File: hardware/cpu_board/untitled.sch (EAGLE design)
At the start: 75 parts, among them IC1 MAX232ECWE, IC2 MAX232ECWE, IC3 AM29F040J, IC4 74HCT138D, IC5 LM2596S, IC6 74HCT273DW, IC7 74LVC1G08DBV, IC8 74LVC1G04DBV, J2 POWER_JACKSLT, U1 AS6C4008-55SIN

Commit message: RAM/ROM address decoder (work in progress)
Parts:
- added IC9: 74HCT138D, 74xx-eu:74HCT138D
- added LED1: (no value), led:LEDCHIP-LED0603
- added R17, R18: (no value), rcl:R-EU_R0603
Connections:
- new net N$46: IC6A.Q4, R17.2
- new net N$47: LED1.A, R17.1
- new net N$48: IC9A.G1, R18.1
- net !MEMEN: now also IC9A.G2A
- net !RAM_CS: now also IC9A.Y2, IC9A.Y4, IC9A.Y5
- net !ROM_CS: now also IC9A.Y0
- net 5V: now also IC9P.VCC, R18.2
- net GND: now also IC9A.A, IC9A.G2B, IC9P.GND, LED1.C
- net ROMSHADOW: now also IC9A.B
- net _A15: now also IC9A.C
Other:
- moved on the sheet: R16
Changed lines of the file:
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@@
 <part name="R16" library="rcl" deviceset="R-EU_" device="R0603"/>
 <part name="IC7" library="74xx-little-de" deviceset="74*1G08" device="DBV" technology="LVC"/>
+<part name="R17" library="rcl" deviceset="R-EU_" device="R0603"/>
+<part name="LED1" library="led" deviceset="LED" device="CHIP-LED0603"/>
+<part name="GND22" library="supply1" deviceset="GND" device=""/>
+<part name="IC9" library="74xx-eu" deviceset="74*138" device="D" technology="HCT"/>
+<part name="GND23" library="supply1" deviceset="GND" device=""/>
+<part name="R18" library="rcl" deviceset="R-EU_" device="R0603"/>
 </parts>
 <sheets>
@@
 <instance part="IC8" gate="A" x="182.88" y="274.32"/>
 <instance part="IC8" gate="P" x="25.4" y="190.5"/>
-<instance part="R16" gate="G$1" x="-220.98" y="-50.8"/>
+<instance part="R16" gate="G$1" x="-210.82" y="-38.1"/>
 <instance part="IC7" gate="A" x="203.2" y="271.78"/>
 <instance part="IC7" gate="P" x="35.56" y="190.5"/>
+<instance part="R17" gate="G$1" x="284.48" y="287.02" rot="R180"/>
+<instance part="LED1" gate="G$1" x="294.64" y="287.02" rot="R90"/>
+<instance part="GND22" gate="1" x="302.26" y="281.94"/>
+<instance part="IC9" gate="A" x="-182.88" y="-40.64"/>
+<instance part="GND23" gate="1" x="-203.2" y="-55.88"/>
+<instance part="R18" gate="G$1" x="-200.66" y="-25.4" rot="R90"/>
+<instance part="IC9" gate="P" x="45.72" y="190.5"/>
 </instances>
 <busses>
@@
 <wire x1="35.56" y1="180.34" x2="35.56" y2="182.88" width="0.1524" layer="91"/>
 <junction x="25.4" y="180.34"/>
+<pinref part="IC9" gate="P" pin="GND"/>
+<wire x1="35.56" y1="180.34" x2="45.72" y2="180.34" width="0.1524" layer="91"/>
+<wire x1="45.72" y1="180.34" x2="45.72" y2="182.88" width="0.1524" layer="91"/>
+<junction x="35.56" y="180.34"/>
 </segment>
 <segment>
@@
 <junction x="248.92" y="276.86"/>
 </segment>
+<segment>
+<pinref part="LED1" gate="G$1" pin="C"/>
+<pinref part="GND22" gate="1" pin="GND"/>
+<wire x1="299.72" y1="287.02" x2="302.26" y2="287.02" width="0.1524" layer="91"/>
+<wire x1="302.26" y1="287.02" x2="302.26" y2="284.48" width="0.1524" layer="91"/>
+</segment>
+<segment>
+<pinref part="IC9" gate="A" pin="A"/>
+<pinref part="GND23" gate="1" pin="GND"/>
+<wire x1="-198.12" y1="-33.02" x2="-203.2" y2="-33.02" width="0.1524" layer="91"/>
+<wire x1="-203.2" y1="-33.02" x2="-203.2" y2="-50.8" width="0.1524" layer="91"/>
+<pinref part="IC9" gate="A" pin="G2B"/>
+<wire x1="-203.2" y1="-50.8" x2="-203.2" y2="-53.34" width="0.1524" layer="91"/>
+<wire x1="-198.12" y1="-50.8" x2="-203.2" y2="-50.8" width="0.1524" layer="91"/>
+<junction x="-203.2" y="-50.8"/>
+</segment>
 </net>
 <net name="5V" class="0">
@@
 <wire x1="35.56" y1="200.66" x2="35.56" y2="198.12" width="0.1524" layer="91"/>
 <junction x="25.4" y="200.66"/>
+<pinref part="IC9" gate="P" pin="VCC"/>
+<wire x1="35.56" y1="200.66" x2="45.72" y2="200.66" width="0.1524" layer="91"/>
+<wire x1="45.72" y1="200.66" x2="45.72" y2="198.12" width="0.1524" layer="91"/>
+<junction x="35.56" y="200.66"/>
 </segment>
 <segment>
@@
 <wire x1="-220.98" y1="35.56" x2="-220.98" y2="38.1" width="0.1524" layer="91"/>
 </segment>
+<segment>
+<pinref part="R18" gate="G$1" pin="2"/>
+<wire x1="-200.66" y1="-20.32" x2="-200.66" y2="-15.24" width="0.1524" layer="91"/>
+</segment>
 </net>
 <net name="TXD1" class="0">
@@
 <segment>
 <pinref part="R16" gate="G$1" pin="1"/>
-<wire x1="-226.06" y1="-50.8" x2="-228.6" y2="-50.8" width="0.1524" layer="91"/>
+<wire x1="-215.9" y1="-38.1" x2="-218.44" y2="-38.1" width="0.1524" layer="91"/>
 </segment>
 </net>
@@
 <label x="373.38" y="5.08" size="1.4224" layer="95" rot="R180" xref="yes"/>
 </segment>
+<segment>
+<pinref part="IC9" gate="A" pin="Y0"/>
+<wire x1="-170.18" y1="-33.02" x2="-165.1" y2="-33.02" width="0.1524" layer="91"/>
+</segment>
 </net>
 <net name="!RAM_CS" class="0">
@@
 <wire x1="271.78" y1="50.8" x2="266.7" y2="50.8" width="0.1524" layer="91"/>
 <label x="266.7" y="50.8" size="1.4224" layer="95" rot="R180" xref="yes"/>
+</segment>
+<segment>
+<pinref part="IC9" gate="A" pin="Y2"/>
+<wire x1="-170.18" y1="-38.1" x2="-167.64" y2="-38.1" width="0.1524" layer="91"/>
+<wire x1="-167.64" y1="-38.1" x2="-167.64" y2="-43.18" width="0.1524" layer="91"/>
+<pinref part="IC9" gate="A" pin="Y4"/>
+<wire x1="-167.64" y1="-43.18" x2="-170.18" y2="-43.18" width="0.1524" layer="91"/>
+<pinref part="IC9" gate="A" pin="Y5"/>
+<wire x1="-170.18" y1="-45.72" x2="-167.64" y2="-45.72" width="0.1524" layer="91"/>
+<wire x1="-167.64" y1="-45.72" x2="-167.64" y2="-43.18" width="0.1524" layer="91"/>
+<junction x="-167.64" y="-43.18"/>
+<wire x1="-167.64" y1="-43.18" x2="-162.56" y2="-43.18" width="0.1524" layer="91"/>
 </segment>
 </net>
@@
 <wire x1="104.14" y1="317.5" x2="104.14" y2="325.12" width="0.1524" layer="91"/>
 </segment>
+<segment>
+<pinref part="IC9" gate="A" pin="G2A"/>
+<wire x1="-198.12" y1="-48.26" x2="-205.74" y2="-48.26" width="0.1524" layer="91"/>
+</segment>
 </net>
 <net name="ROMSHADOW" class="0">
@@
 <wire x1="276.86" y1="289.56" x2="284.48" y2="289.56" width="0.1524" layer="91"/>
 </segment>
+<segment>
+<pinref part="IC9" gate="A" pin="B"/>
+<wire x1="-198.12" y1="-35.56" x2="-205.74" y2="-35.56" width="0.1524" layer="91"/>
+</segment>
 </net>
 <net name="_A15" class="0">
 <segment>
 <pinref part="R16" gate="G$1" pin="2"/>
-<wire x1="-208.28" y1="-50.8" x2="-215.9" y2="-50.8" width="0.1524" layer="91"/>
+<wire x1="-198.12" y1="-38.1" x2="-205.74" y2="-38.1" width="0.1524" layer="91"/>
+<pinref part="IC9" gate="A" pin="C"/>
 </segment>
 </net>
@@
 </segment>
 </net>
+<net name="N$46" class="0">
+<segment>
+<pinref part="IC6" gate="A" pin="Q4"/>
+<pinref part="R17" gate="G$1" pin="2"/>
+<wire x1="279.4" y1="287.02" x2="276.86" y2="287.02" width="0.1524" layer="91"/>
+</segment>
+</net>
+<net name="N$47" class="0">
+<segment>
+<pinref part="R17" gate="G$1" pin="1"/>
+<pinref part="LED1" gate="G$1" pin="A"/>
+<wire x1="292.1" y1="287.02" x2="289.56" y2="287.02" width="0.1524" layer="91"/>
+</segment>
+</net>
+<net name="N$48" class="0">
+<segment>
+<pinref part="IC9" gate="A" pin="G1"/>
+<pinref part="R18" gate="G$1" pin="1"/>
+<wire x1="-198.12" y1="-45.72" x2="-200.66" y2="-45.72" width="0.1524" layer="91"/>
+<wire x1="-200.66" y1="-45.72" x2="-200.66" y2="-30.48" width="0.1524" layer="91"/>
+</segment>
+</net>

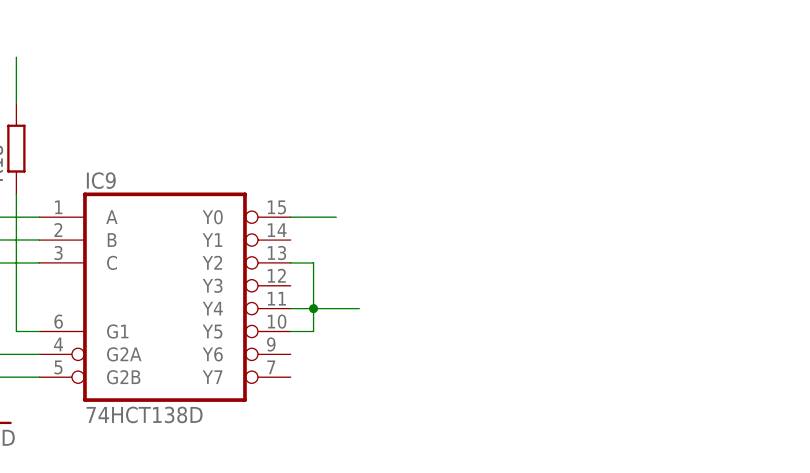
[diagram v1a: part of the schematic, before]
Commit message: ROM/RAM address decoder (version with diodes and wired-or on RAMCS line)
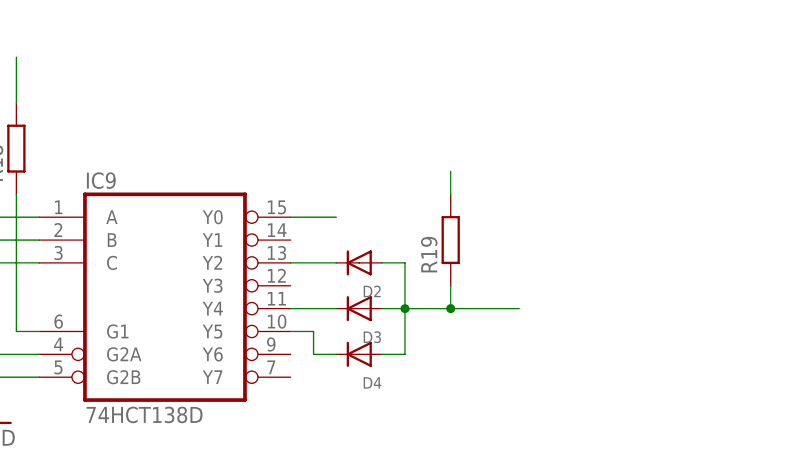
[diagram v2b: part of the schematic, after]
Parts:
- added D2, D3, D4: (no value), adafruit:DIODESOD-323
- added R19: (no value), rcl:R-EU_R0603
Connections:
- new net N$49: D2.C, IC9A.Y2
- new net N$50: D4.C, IC9A.Y5
- new net N$51: D3.C, IC9A.Y4
- net !RAM_CS: now also D2.A, D3.A, D4.A, R19.1; no longer IC9A.Y2, IC9A.Y4, IC9A.Y5
- net 5V: now also R19.2
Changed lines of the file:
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@@
 <part name="GND23" library="supply1" deviceset="GND" device=""/>
 <part name="R18" library="rcl" deviceset="R-EU_" device="R0603"/>
+<part name="D2" library="adafruit" deviceset="DIODE" device="SOD-323"/>
+<part name="D3" library="adafruit" deviceset="DIODE" device="SOD-323"/>
+<part name="D4" library="adafruit" deviceset="DIODE" device="SOD-323"/>
+<part name="R19" library="rcl" deviceset="R-EU_" device="R0603"/>
 </parts>
 <sheets>
@@
 <instance part="R18" gate="G$1" x="-200.66" y="-25.4" rot="R90"/>
 <instance part="IC9" gate="P" x="45.72" y="190.5"/>
+<instance part="D2" gate="G$1" x="-162.56" y="-38.1" rot="R180"/>
+<instance part="D3" gate="G$1" x="-162.56" y="-43.18" rot="R180"/>
+<instance part="D4" gate="G$1" x="-162.56" y="-48.26" rot="R180"/>
+<instance part="R19" gate="G$1" x="-152.4" y="-35.56" rot="R90"/>
 </instances>
 <busses>
@@
 <wire x1="-200.66" y1="-20.32" x2="-200.66" y2="-15.24" width="0.1524" layer="91"/>
 </segment>
+<segment>
+<pinref part="R19" gate="G$1" pin="2"/>
+<wire x1="-152.4" y1="-30.48" x2="-152.4" y2="-27.94" width="0.1524" layer="91"/>
+</segment>
 </net>
 <net name="TXD1" class="0">
@@
 </segment>
 <segment>
-<pinref part="IC9" gate="A" pin="Y2"/>
-<wire x1="-170.18" y1="-38.1" x2="-167.64" y2="-38.1" width="0.1524" layer="91"/>
-<wire x1="-167.64" y1="-38.1" x2="-167.64" y2="-43.18" width="0.1524" layer="91"/>
-<pinref part="IC9" gate="A" pin="Y4"/>
-<wire x1="-167.64" y1="-43.18" x2="-170.18" y2="-43.18" width="0.1524" layer="91"/>
-<pinref part="IC9" gate="A" pin="Y5"/>
-<wire x1="-170.18" y1="-45.72" x2="-167.64" y2="-45.72" width="0.1524" layer="91"/>
-<wire x1="-167.64" y1="-45.72" x2="-167.64" y2="-43.18" width="0.1524" layer="91"/>
-<junction x="-167.64" y="-43.18"/>
-<wire x1="-167.64" y1="-43.18" x2="-162.56" y2="-43.18" width="0.1524" layer="91"/>
+<pinref part="D2" gate="G$1" pin="A"/>
+<wire x1="-160.02" y1="-38.1" x2="-157.48" y2="-38.1" width="0.1524" layer="91"/>
+<wire x1="-157.48" y1="-38.1" x2="-157.48" y2="-43.18" width="0.1524" layer="91"/>
+<pinref part="D4" gate="G$1" pin="A"/>
+<wire x1="-157.48" y1="-43.18" x2="-157.48" y2="-48.26" width="0.1524" layer="91"/>
+<wire x1="-160.02" y1="-48.26" x2="-157.48" y2="-48.26" width="0.1524" layer="91"/>
+<pinref part="D3" gate="G$1" pin="A"/>
+<wire x1="-160.02" y1="-43.18" x2="-157.48" y2="-43.18" width="0.1524" layer="91"/>
+<junction x="-157.48" y="-43.18"/>
+<wire x1="-144.78" y1="-43.18" x2="-152.4" y2="-43.18" width="0.1524" layer="91"/>
+<pinref part="R19" gate="G$1" pin="1"/>
+<wire x1="-152.4" y1="-43.18" x2="-157.48" y2="-43.18" width="0.1524" layer="91"/>
+<wire x1="-152.4" y1="-40.64" x2="-152.4" y2="-43.18" width="0.1524" layer="91"/>
+<junction x="-152.4" y="-43.18"/>
 </segment>
 </net>
@@
 </segment>
 </net>
+<net name="N$49" class="0">
+<segment>
+<pinref part="IC9" gate="A" pin="Y2"/>
+<pinref part="D2" gate="G$1" pin="C"/>
+<wire x1="-165.1" y1="-38.1" x2="-170.18" y2="-38.1" width="0.1524" layer="91"/>
+</segment>
+</net>
+<net name="N$50" class="0">
+<segment>
+<pinref part="IC9" gate="A" pin="Y5"/>
+<wire x1="-170.18" y1="-45.72" x2="-167.64" y2="-45.72" width="0.1524" layer="91"/>
+<wire x1="-167.64" y1="-45.72" x2="-167.64" y2="-48.26" width="0.1524" layer="91"/>
+<pinref part="D4" gate="G$1" pin="C"/>
+<wire x1="-167.64" y1="-48.26" x2="-165.1" y2="-48.26" width="0.1524" layer="91"/>
+</segment>
+</net>
+<net name="N$51" class="0">
+<segment>
+<pinref part="IC9" gate="A" pin="Y4"/>
+<pinref part="D3" gate="G$1" pin="C"/>
+<wire x1="-170.18" y1="-43.18" x2="-165.1" y2="-43.18" width="0.1524" layer="91"/>
+</segment>
+</net>

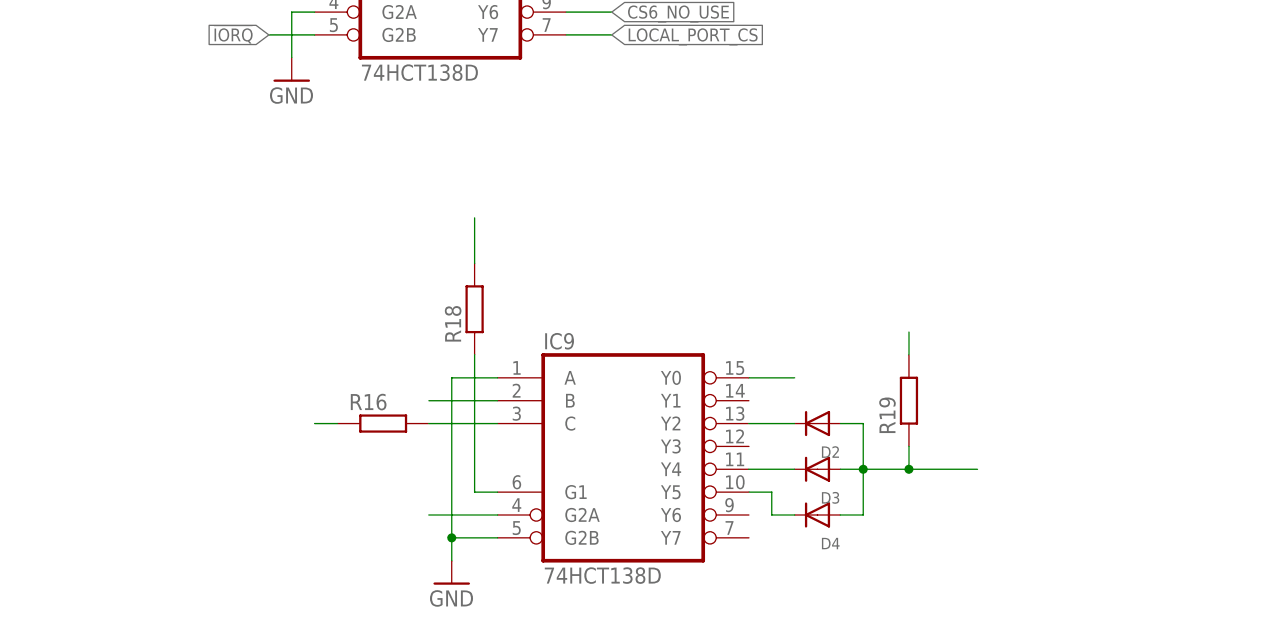
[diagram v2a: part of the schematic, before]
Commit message: ROM/RAM address decoder bug fix
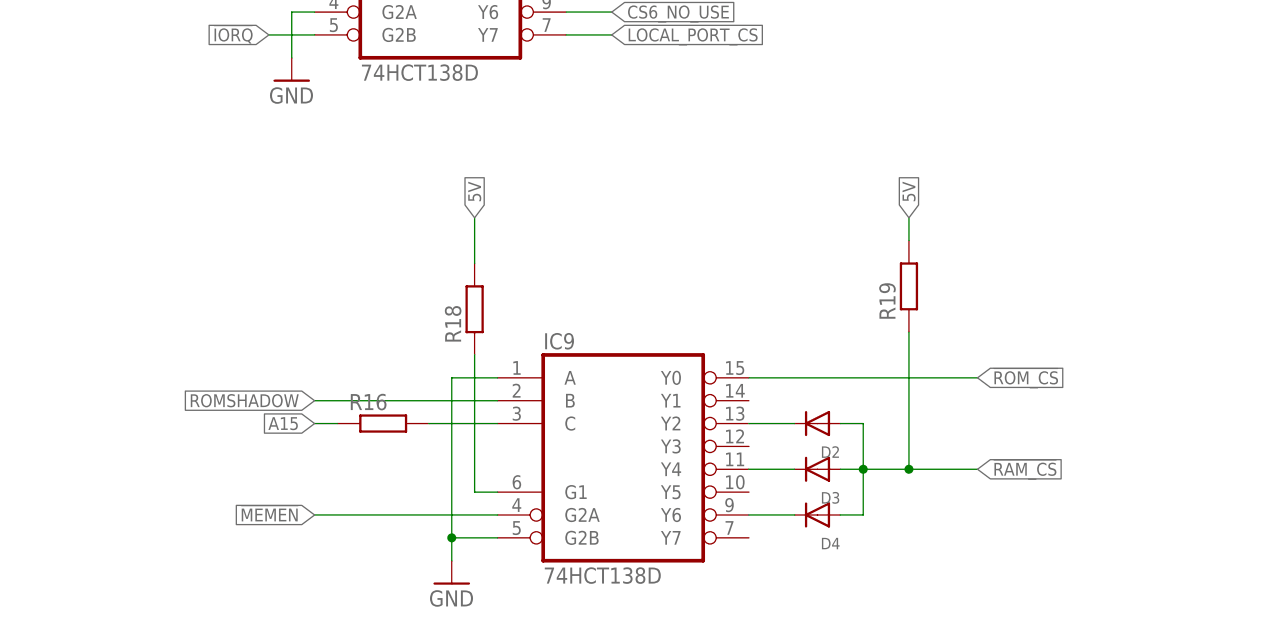
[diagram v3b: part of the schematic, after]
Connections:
- net N$50: now also IC9A.Y6; no longer IC9A.Y5
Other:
- moved on the sheet: R19
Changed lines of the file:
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@@
 <instance part="D3" gate="G$1" x="-162.56" y="-43.18" rot="R180"/>
 <instance part="D4" gate="G$1" x="-162.56" y="-48.26" rot="R180"/>
-<instance part="R19" gate="G$1" x="-152.4" y="-35.56" rot="R90"/>
+<instance part="R19" gate="G$1" x="-152.4" y="-22.86" rot="R90"/>
 </instances>
 <busses>
@@
 <pinref part="R18" gate="G$1" pin="2"/>
 <wire x1="-200.66" y1="-20.32" x2="-200.66" y2="-15.24" width="0.1524" layer="91"/>
+<label x="-200.66" y="-15.24" size="1.4224" layer="95" rot="R90" xref="yes"/>
 </segment>
 <segment>
 <pinref part="R19" gate="G$1" pin="2"/>
-<wire x1="-152.4" y1="-30.48" x2="-152.4" y2="-27.94" width="0.1524" layer="91"/>
+<wire x1="-152.4" y1="-17.78" x2="-152.4" y2="-15.24" width="0.1524" layer="91"/>
+<label x="-152.4" y="-15.24" size="1.4224" layer="95" rot="R90" xref="yes"/>
 </segment>
 </net>
@@
 <pinref part="R16" gate="G$1" pin="1"/>
 <wire x1="-215.9" y1="-38.1" x2="-218.44" y2="-38.1" width="0.1524" layer="91"/>
+<label x="-218.44" y="-38.1" size="1.4224" layer="95" rot="R180" xref="yes"/>
 </segment>
 </net>
@@
 <segment>
 <pinref part="IC9" gate="A" pin="Y0"/>
-<wire x1="-170.18" y1="-33.02" x2="-165.1" y2="-33.02" width="0.1524" layer="91"/>
+<wire x1="-170.18" y1="-33.02" x2="-144.78" y2="-33.02" width="0.1524" layer="91"/>
+<label x="-144.78" y="-33.02" size="1.4224" layer="95" xref="yes"/>
 </segment>
 </net>
@@
 <pinref part="R19" gate="G$1" pin="1"/>
 <wire x1="-152.4" y1="-43.18" x2="-157.48" y2="-43.18" width="0.1524" layer="91"/>
-<wire x1="-152.4" y1="-40.64" x2="-152.4" y2="-43.18" width="0.1524" layer="91"/>
+<wire x1="-152.4" y1="-27.94" x2="-152.4" y2="-43.18" width="0.1524" layer="91"/>
 <junction x="-152.4" y="-43.18"/>
+<label x="-144.78" y="-43.18" size="1.4224" layer="95" xref="yes"/>
 </segment>
 </net>
@@
 <segment>
 <pinref part="IC9" gate="A" pin="G2A"/>
-<wire x1="-198.12" y1="-48.26" x2="-205.74" y2="-48.26" width="0.1524" layer="91"/>
+<wire x1="-198.12" y1="-48.26" x2="-218.44" y2="-48.26" width="0.1524" layer="91"/>
+<label x="-218.44" y="-48.26" size="1.4224" layer="95" rot="R180" xref="yes"/>
 </segment>
 </net>
@@
 <segment>
 <pinref part="IC9" gate="A" pin="B"/>
-<wire x1="-198.12" y1="-35.56" x2="-205.74" y2="-35.56" width="0.1524" layer="91"/>
+<wire x1="-198.12" y1="-35.56" x2="-218.44" y2="-35.56" width="0.1524" layer="91"/>
+<label x="-218.44" y="-35.56" size="1.4224" layer="95" rot="R180" xref="yes"/>
 </segment>
 </net>
@@
 <net name="N$50" class="0">
 <segment>
-<pinref part="IC9" gate="A" pin="Y5"/>
-<wire x1="-170.18" y1="-45.72" x2="-167.64" y2="-45.72" width="0.1524" layer="91"/>
-<wire x1="-167.64" y1="-45.72" x2="-167.64" y2="-48.26" width="0.1524" layer="91"/>
 <pinref part="D4" gate="G$1" pin="C"/>
-<wire x1="-167.64" y1="-48.26" x2="-165.1" y2="-48.26" width="0.1524" layer="91"/>
-</segment>
-</net>
+<pinref part="IC9" gate="A" pin="Y6"/>
+<wire x1="-165.1" y1="-48.26" x2="-170.18" y2="-48.26" width="0.1524" layer="91"/>
+</segment>
+</net>

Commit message: Capacitor added
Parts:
- removed C15: (no value), rcl:C-EUC0603
- C3: device rcl:C-EUC0402 -> rcl:C-EUC0603
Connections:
- net 5V: no longer C15.1
- net GND: no longer C15.2
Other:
- moved on the sheet: C1, C11, C12, C13, C14, C17, C24, C26, C27, C29, C3, C30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

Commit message: CPU size fixed
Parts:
- U$4: value HD64180 -> HD64180QFP80_; device mw:HD64180 -> mw:HD64180QFP80_
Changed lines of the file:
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@@
 <part name="JP10" library="pinhead" deviceset="PINHD-1X8" device=""/>
 <part name="JP11" library="pinhead" deviceset="PINHD-1X18" device=""/>
-<part name="U$4" library="mw" deviceset="HD64180" device=""/>
+<part name="U$4" library="mw" deviceset="HD64180" device="QFP80_"/>
 <part name="GND9" library="supply1" deviceset="GND" device=""/>
 <part name="U$3" library="crystal" deviceset="ASE" device=""/>
